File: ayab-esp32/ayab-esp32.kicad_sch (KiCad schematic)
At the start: 16 parts

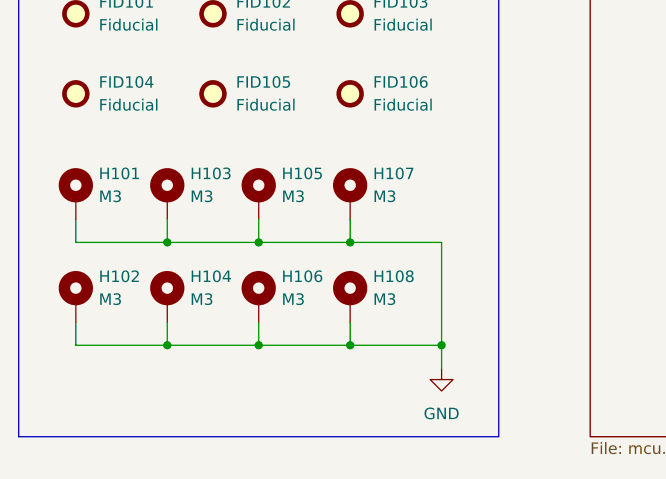
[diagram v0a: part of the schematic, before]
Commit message: Correct footprint and regenerate documentation
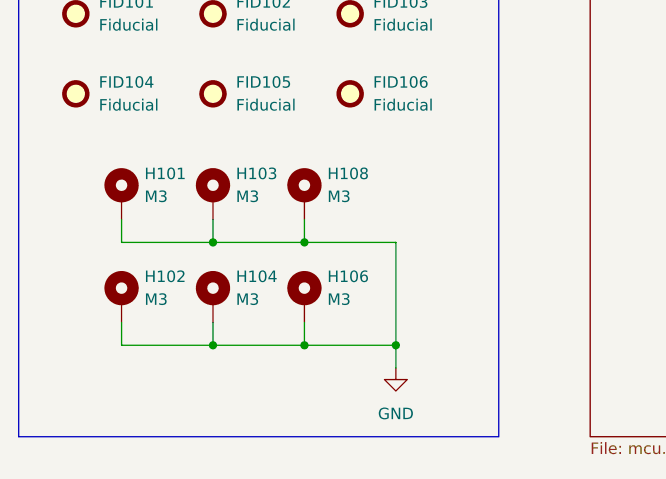
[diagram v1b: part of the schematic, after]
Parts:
- removed H105, H107: M3, MountingHole:MountingHole_2.2mm_M2_DIN965_Pad, symbol ayab-lib:MountingHole_Pad
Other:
- moved on the sheet: H101, H102, H103, H104, H106, H108

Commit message: add mouser parts list
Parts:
- R101, R102: Mouser PN (none) -> 603-AC0603FR-135K1L

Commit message: address bringup issues
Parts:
- H101, H102, H103, H104, H106, H108: footprint MountingHole:MountingHole_2.2mm_M2_DIN965_Pad -> MountingHole:MountingHole_3.2mm_M3_DIN965_Pad
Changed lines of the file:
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@@
 			)
 		)
-		(property "Footprint" "MountingHole:MountingHole_2.2mm_M2_DIN965_Pad"
+		(property "Footprint" "MountingHole:MountingHole_3.2mm_M3_DIN965_Pad"
 			(at 45.72 129.54 0)
 			(effects
@@
 			)
 		)
-		(property "Footprint" "MountingHole:MountingHole_2.2mm_M2_DIN965_Pad"
+		(property "Footprint" "MountingHole:MountingHole_3.2mm_M3_DIN965_Pad"
 			(at 55.88 129.54 0)
 			(effects
@@
 			)
 		)
-		(property "Footprint" "MountingHole:MountingHole_2.2mm_M2_DIN965_Pad"
+		(property "Footprint" "MountingHole:MountingHole_3.2mm_M3_DIN965_Pad"
 			(at 66.04 140.97 0)
 			(effects
@@
 			)
 		)
-		(property "Footprint" "MountingHole:MountingHole_2.2mm_M2_DIN965_Pad"
+		(property "Footprint" "MountingHole:MountingHole_3.2mm_M3_DIN965_Pad"
 			(at 66.04 129.54 0)
 			(effects
@@
 			)
 		)
-		(property "Footprint" "MountingHole:MountingHole_2.2mm_M2_DIN965_Pad"
+		(property "Footprint" "MountingHole:MountingHole_3.2mm_M3_DIN965_Pad"
 			(at 55.88 140.97 0)
 			(effects
@@
 			)
 		)
-		(property "Footprint" "MountingHole:MountingHole_2.2mm_M2_DIN965_Pad"
+		(property "Footprint" "MountingHole:MountingHole_3.2mm_M3_DIN965_Pad"
 			(at 45.72 140.97 0)
 			(effects
